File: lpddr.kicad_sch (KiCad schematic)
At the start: 60 parts, among them U1 MPFS250T-FCVG484, U12 MT53D512M32D2_WFBGA

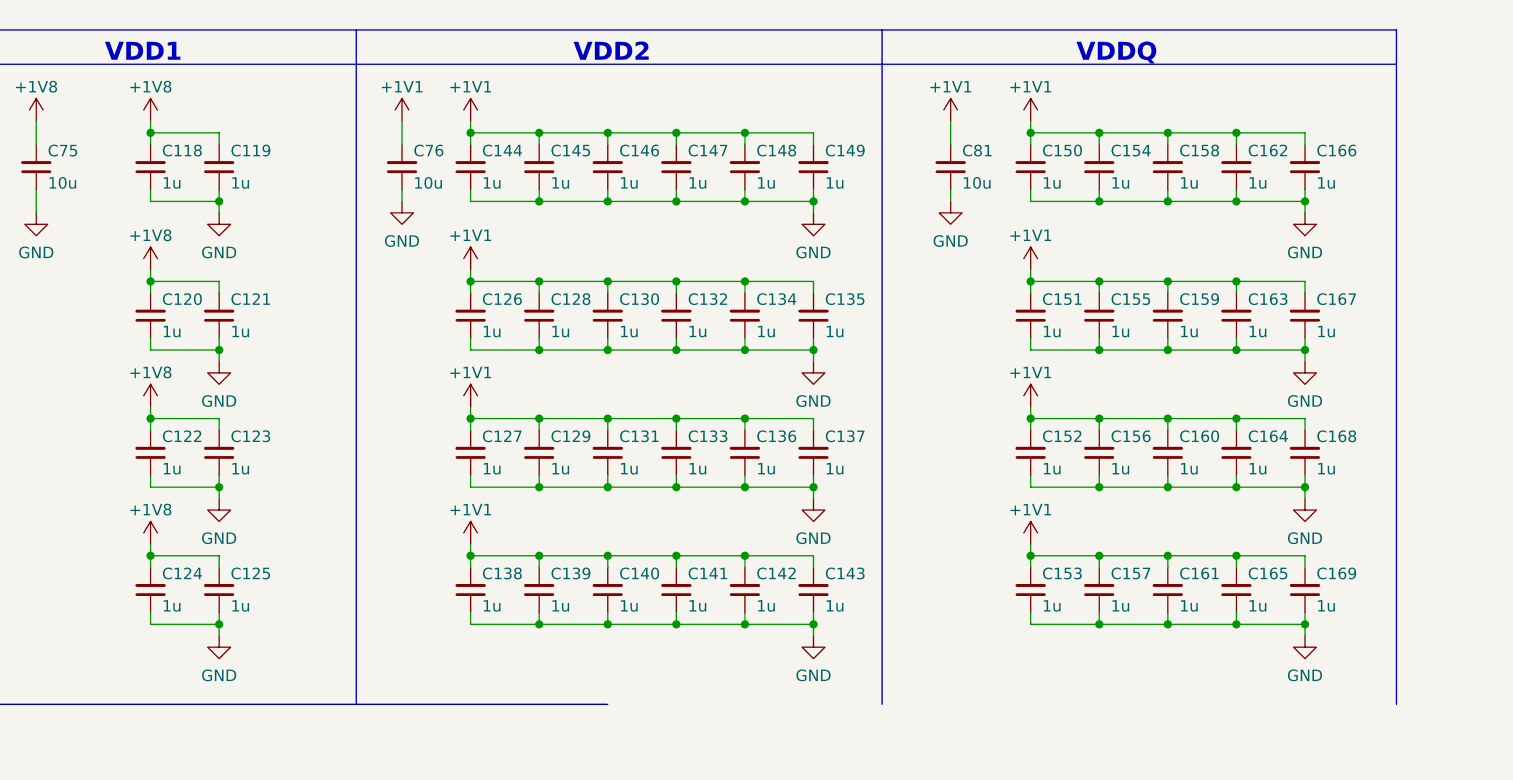
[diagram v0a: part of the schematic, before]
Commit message: [#55992] Replace 100n capacitors
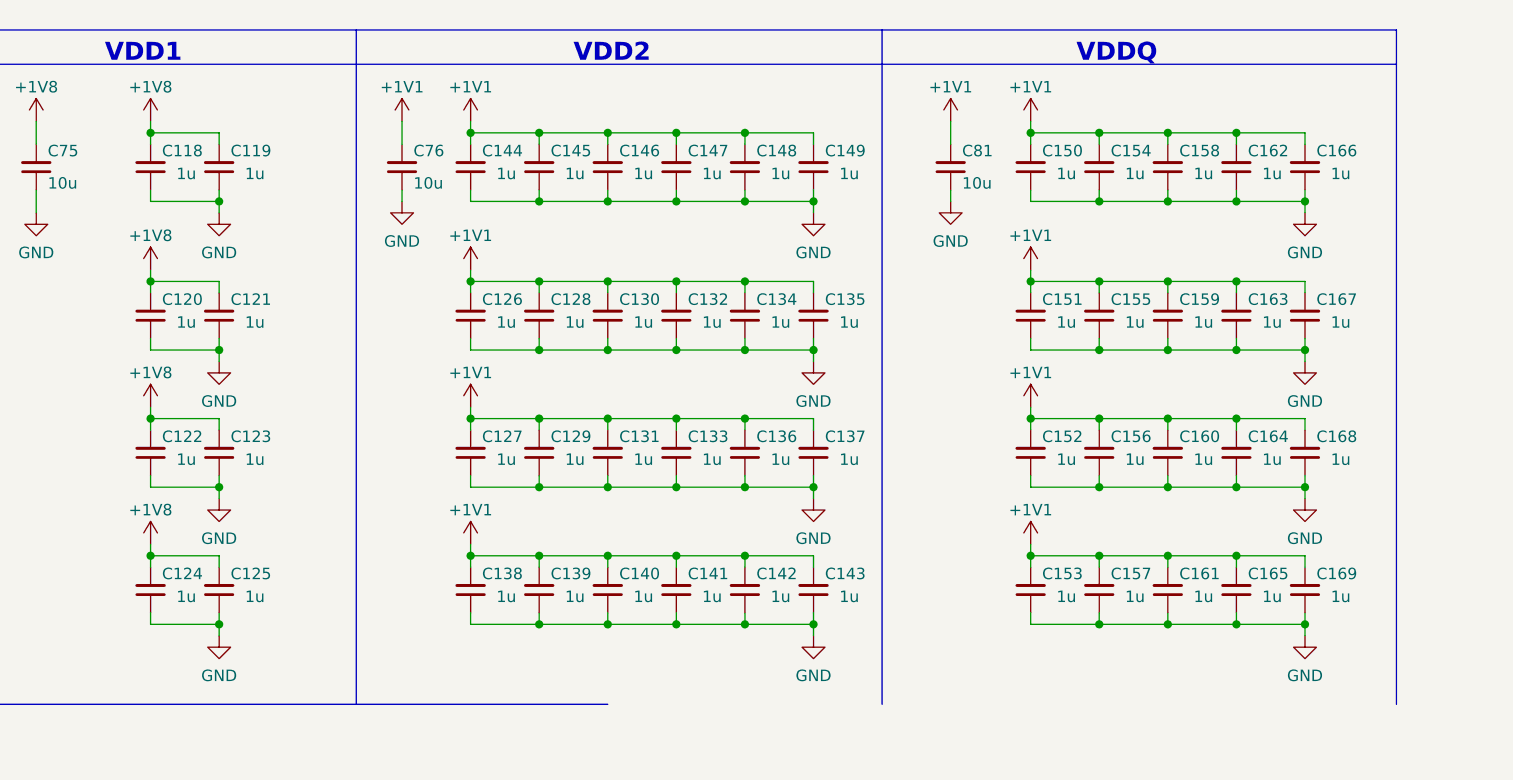
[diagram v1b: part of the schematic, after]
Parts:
- C118, C119, C120, C121, C122, C123, C124, C125, C126, C127, C128, C129, C130, C131, C132, C133, C134, C135, C136, C137, C138, C139, C140, C141, C142, C143, C144, C145, C146, C147, C148, C149, C150, C151, C152, C153, C154, C155, C156, C157, C158, C159, C160, C161, C162, C163, C164, C165, C166, C167, C168, C169: value C_1u_0201 -> C_1u_0402; footprint antmicro-footprints:C_0201 -> antmicro-footprints:C_0402_1005Metric; symbol antmicroCapacitorsmisc:C_1u_0201_16V -> antmicroCapacitors0402:C_1u_0402; MPN GRM033R61C105ME15D -> C1005X6S1A105K050BC; Manufacturer Murata -> TDK

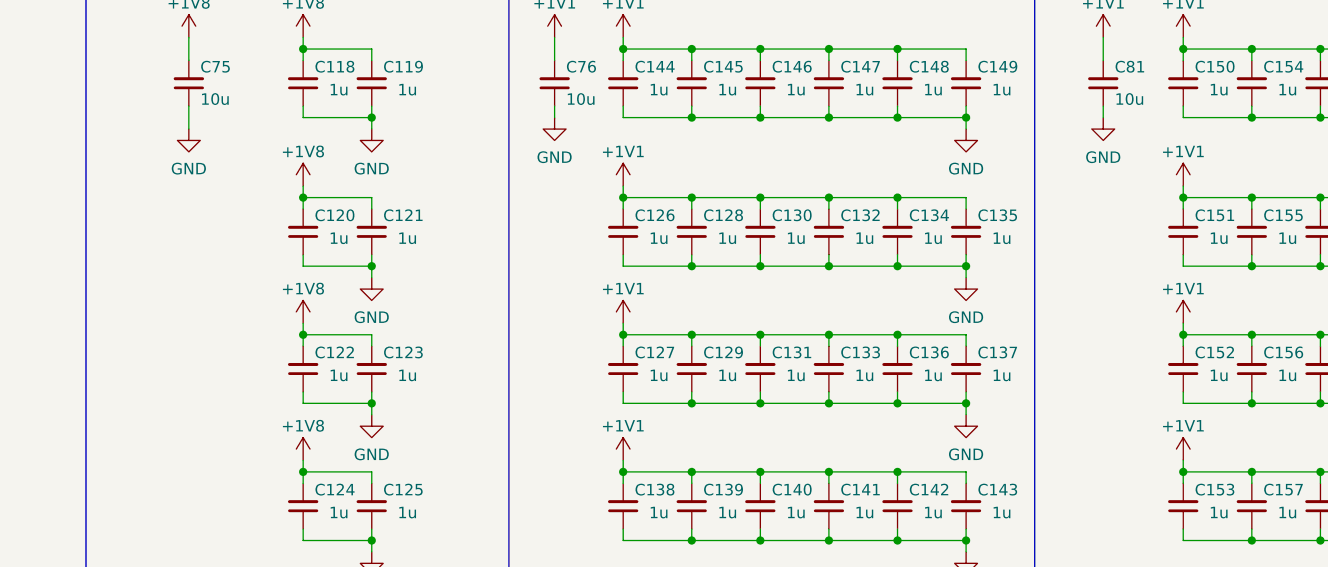
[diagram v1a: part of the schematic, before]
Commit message: [#56060] Place decoupling under LPDDR4
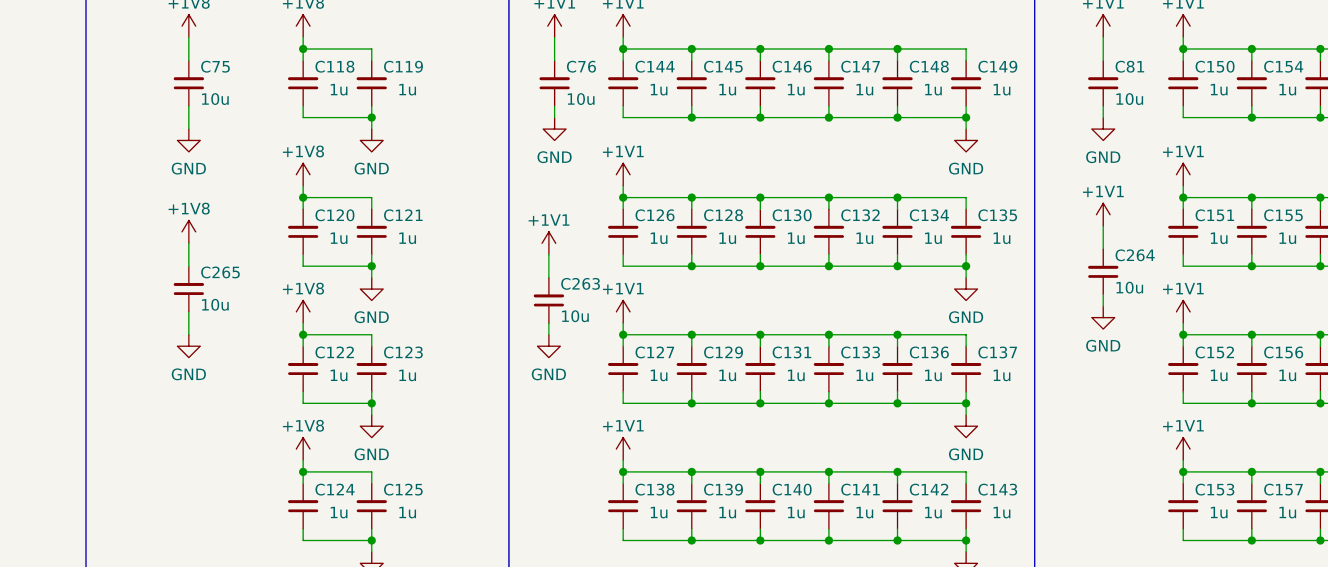
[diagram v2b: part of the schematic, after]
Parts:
- added C263, C264, C265: C_10u_0402, antmicro-footprints:C_0402_1005Metric, symbol antmicroCapacitors0402:C_10u_0402
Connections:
- net +1V1: now also C263.2, C264.2
- net +1V8: now also C265.2
- net GND: now also C263.1, C264.1, C265.1

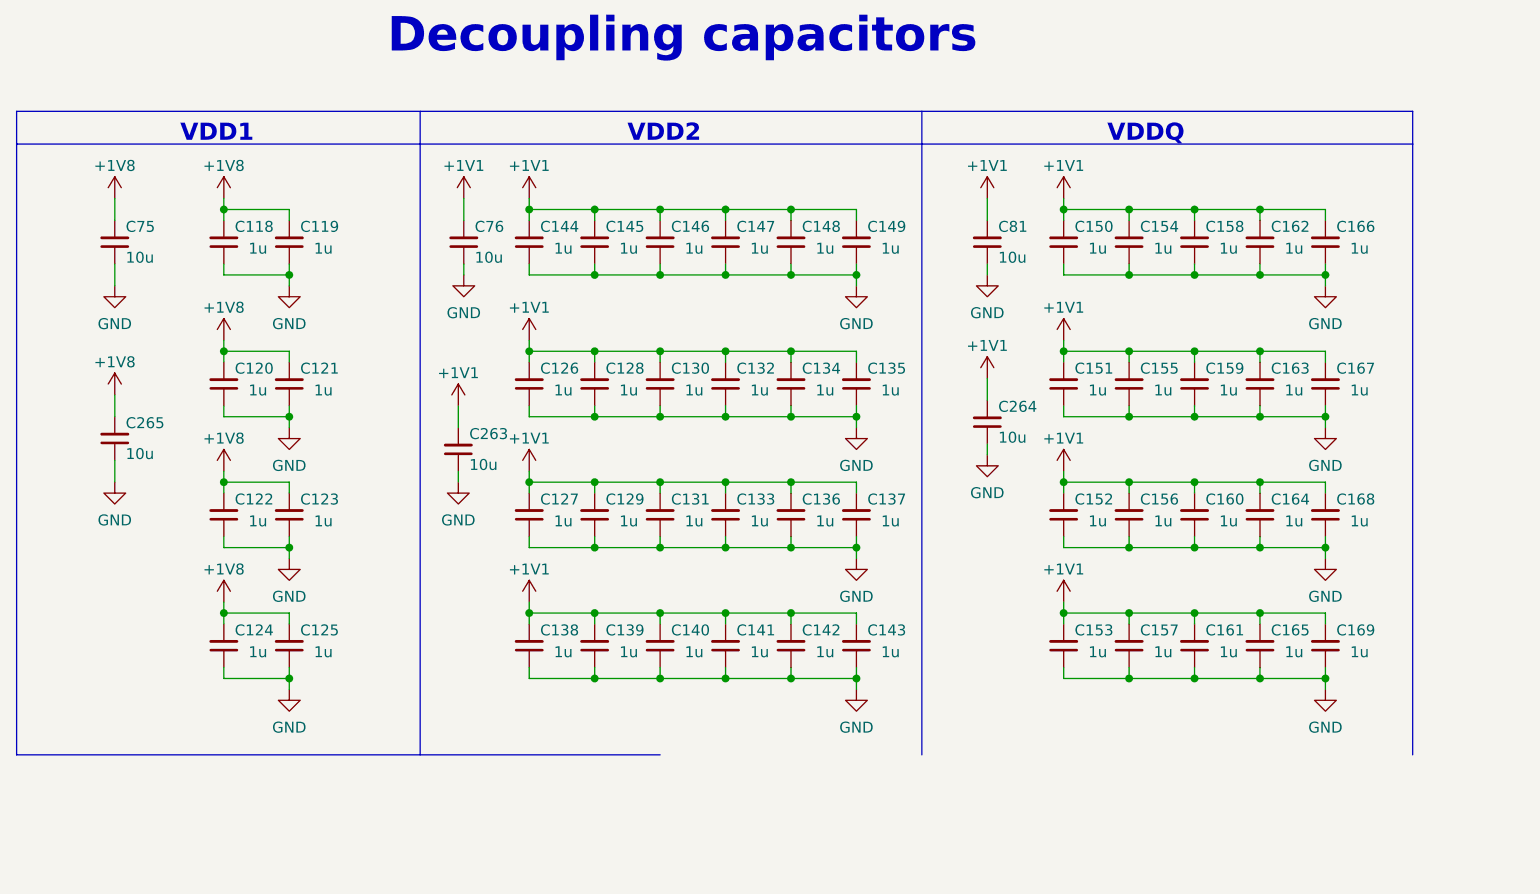
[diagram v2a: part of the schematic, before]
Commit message: [#56060] Reduce decoupling
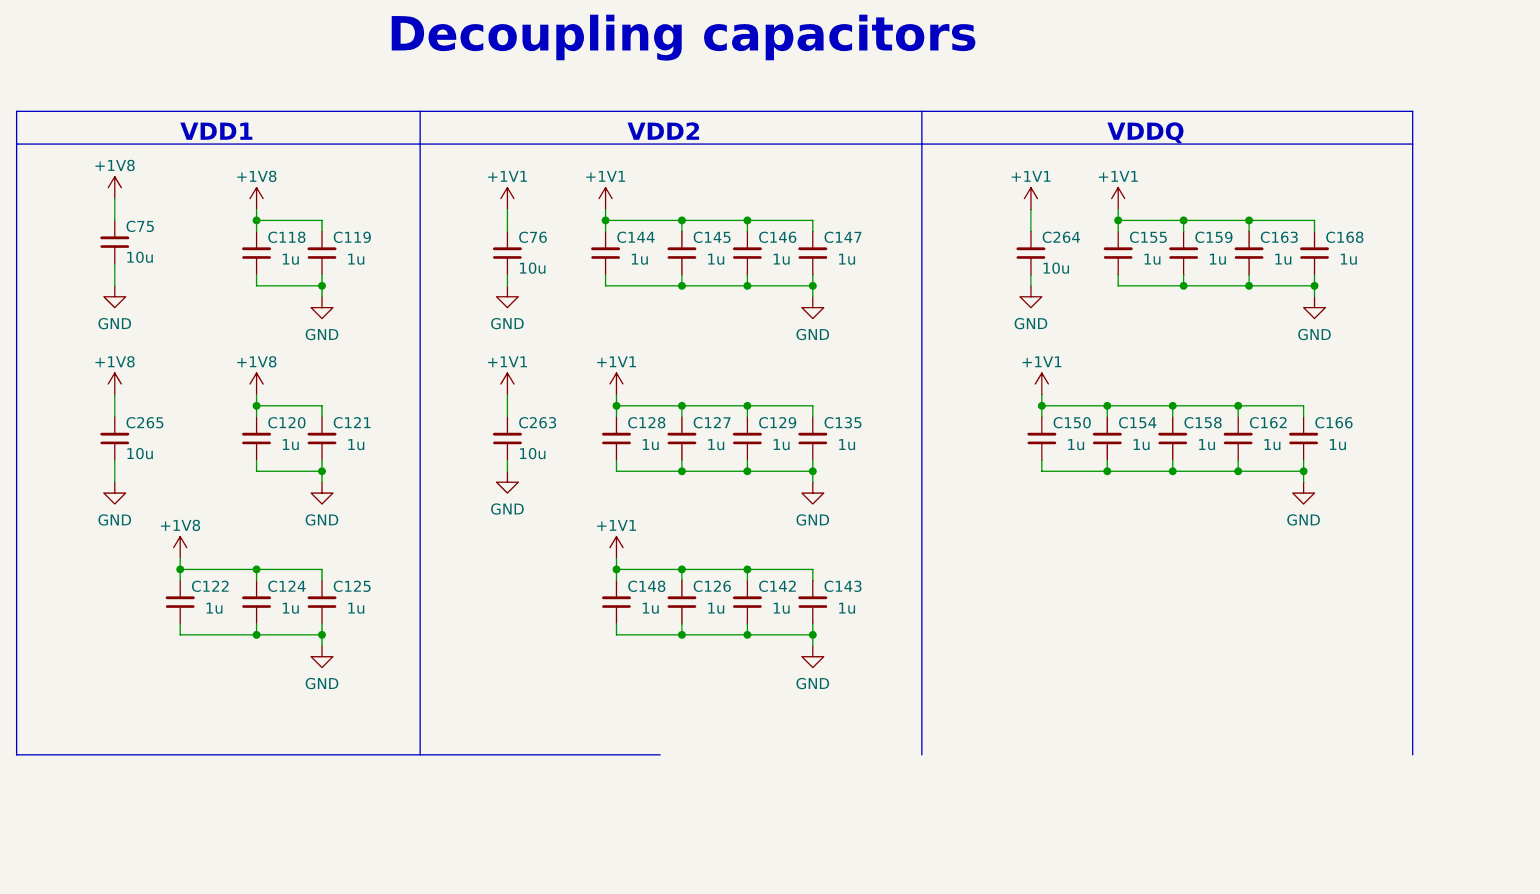
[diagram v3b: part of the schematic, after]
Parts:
- removed C123, C130, C131, C132, C133, C134, C136, C137, C138, C139, C140, C141, C149, C151, C152, C153, C156, C157, C160, C161, C164, C165, C167, C169: C_1u_0402, antmicro-footprints:C_0402_1005Metric, symbol antmicroCapacitors0402:C_1u_0402
- removed C81: C_10u_0402, antmicro-footprints:C_0402_1005Metric, symbol antmicroCapacitors0402:C_10u_0402
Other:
- moved on the sheet: C118, C119, C120, C121, C122, C124, C125, C126, C127, C128, C129, C135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

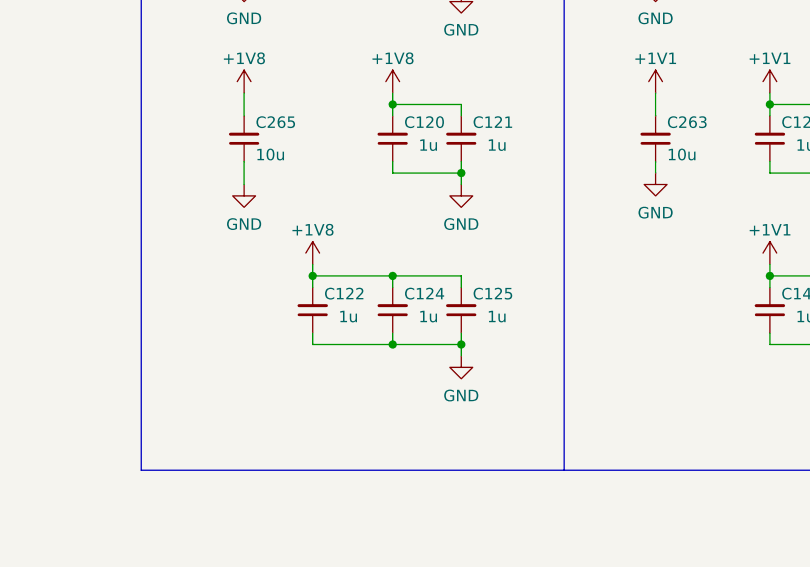
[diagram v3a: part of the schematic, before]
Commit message: [#55992] Place left out components
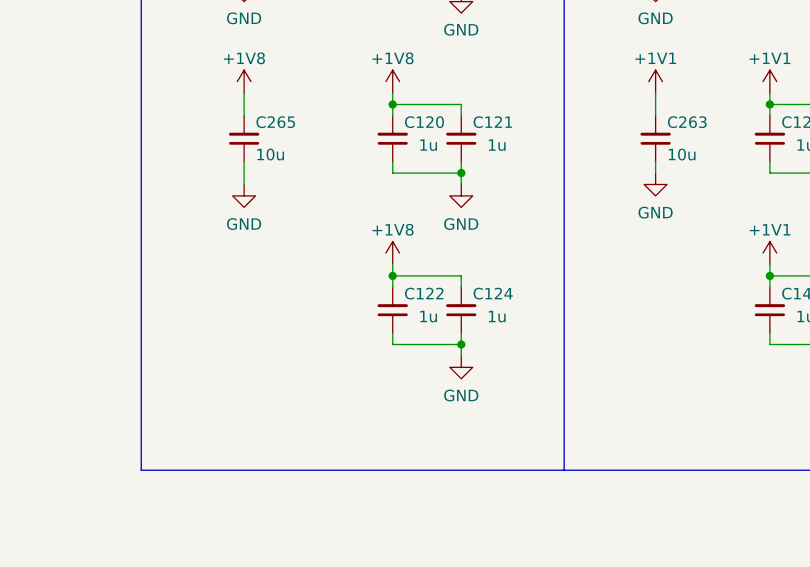
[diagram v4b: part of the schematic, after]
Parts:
- removed C125: C_1u_0402, antmicro-footprints:C_0402_1005Metric, symbol antmicroCapacitors0402:C_1u_0402
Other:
- moved on the sheet: C122, C124
